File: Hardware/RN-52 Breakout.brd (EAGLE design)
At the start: 35.6 x 51.1 mm, 13 parts, among them U1 BLUETOOTH-RN-52

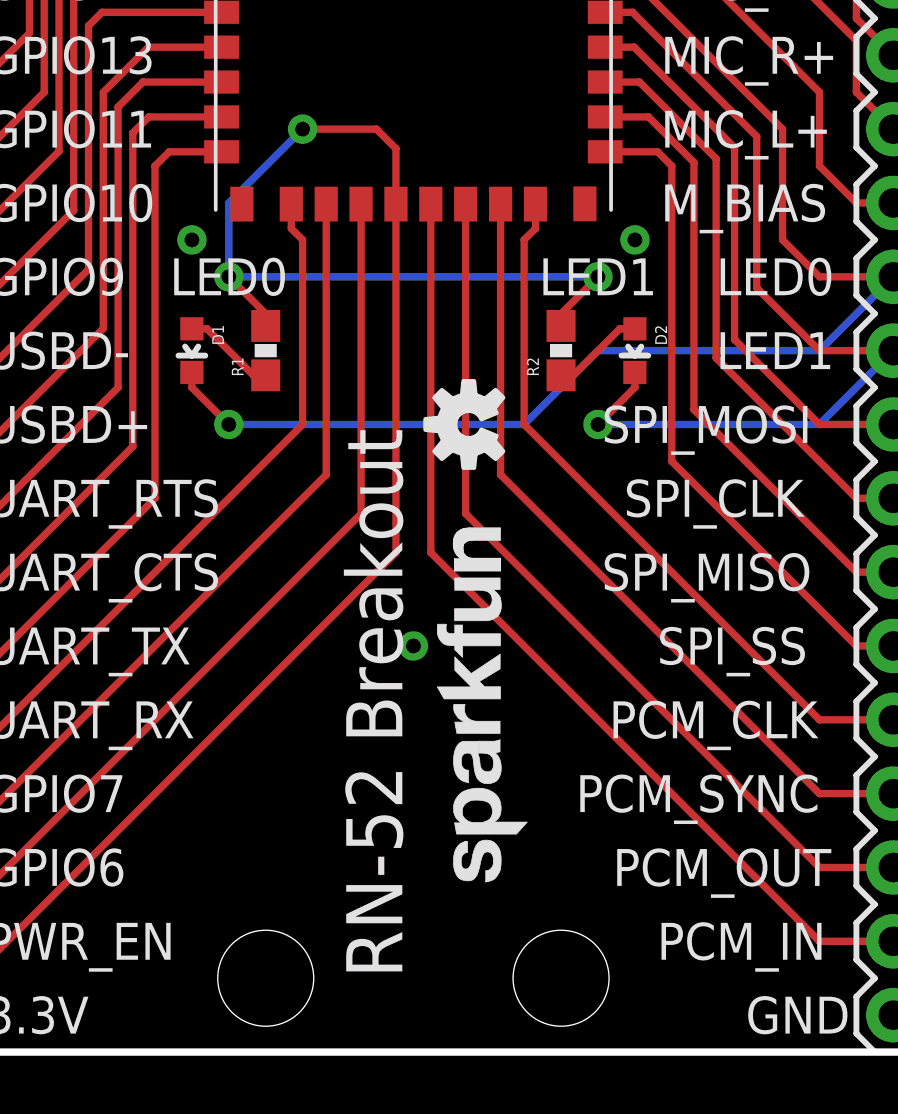
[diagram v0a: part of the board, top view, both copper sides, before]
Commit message: added local fiducials
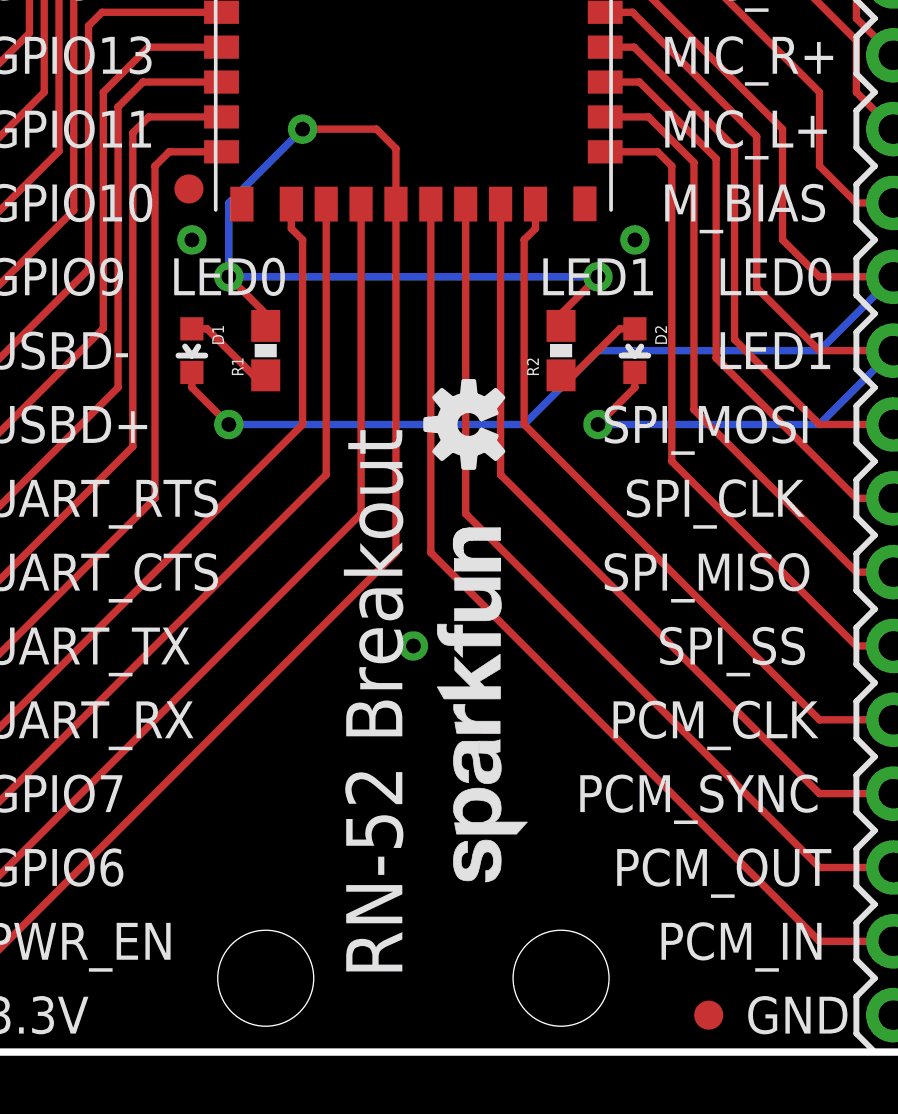
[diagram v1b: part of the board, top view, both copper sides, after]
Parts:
- added FID1, FID2: FIDUCIAL1X2, SparkFun-Aesthetics:FIDUCIAL-1X2
